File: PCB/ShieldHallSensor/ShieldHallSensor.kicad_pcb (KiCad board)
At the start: 2 copper layers, 34.2 x 34.2 mm, 8 parts, among them J1 Shield_Connector_Top_Left, J2 Shield_Connector_Bottom_Left, J3 Shield_Connector_Top_Right, J4 Shield_Connector_Bottom_Right, U1 HallLinearSensor

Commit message: Add smart cube panel
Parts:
- added REF**: Tab, PCM_kikit:Tab, F.Cu at (156.2, 97.0)
- added REF**: Tab, PCM_kikit:Tab, F.Cu at (138.9, 79.7)
- added REF**: Tab, PCM_kikit:Tab, F.Cu at (138.9, 114.3)
- added REF**: Tab, PCM_kikit:Tab, F.Cu at (121.6, 97.0)

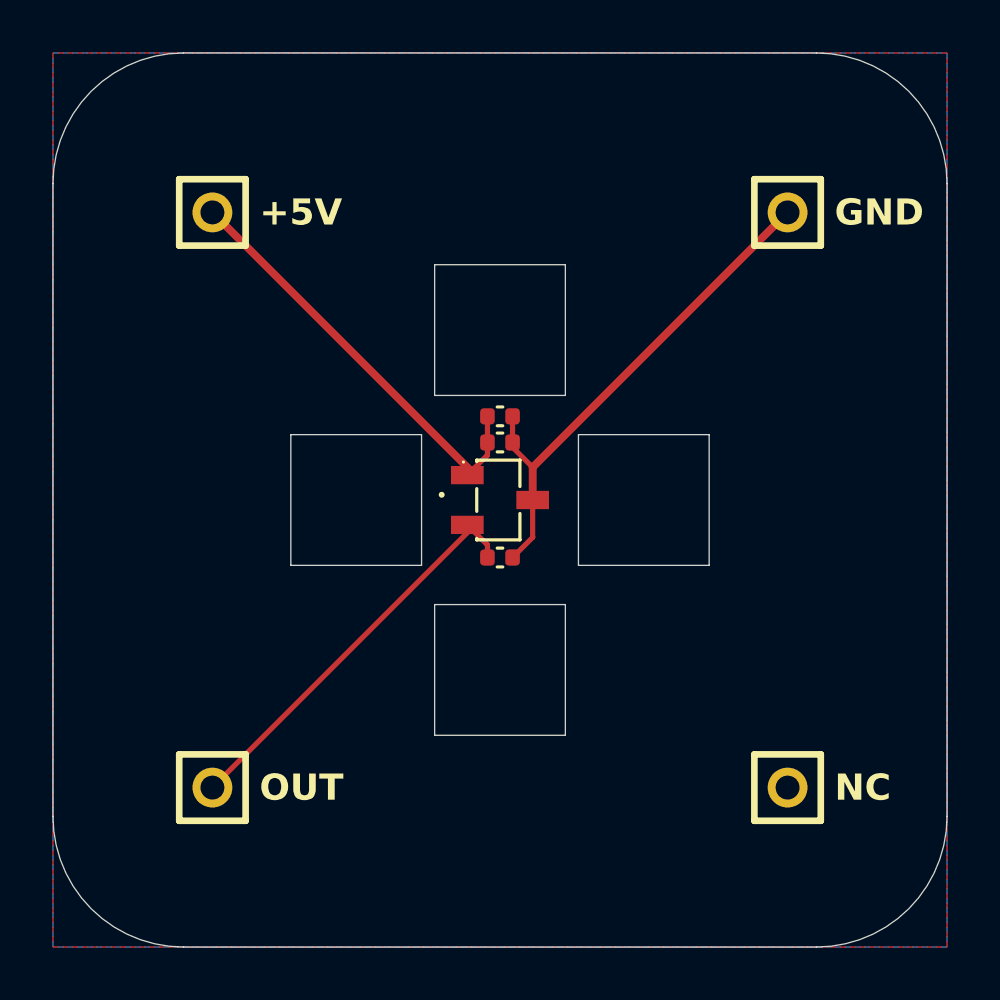
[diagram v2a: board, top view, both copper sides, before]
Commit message: Add power supply (wip) and update panel
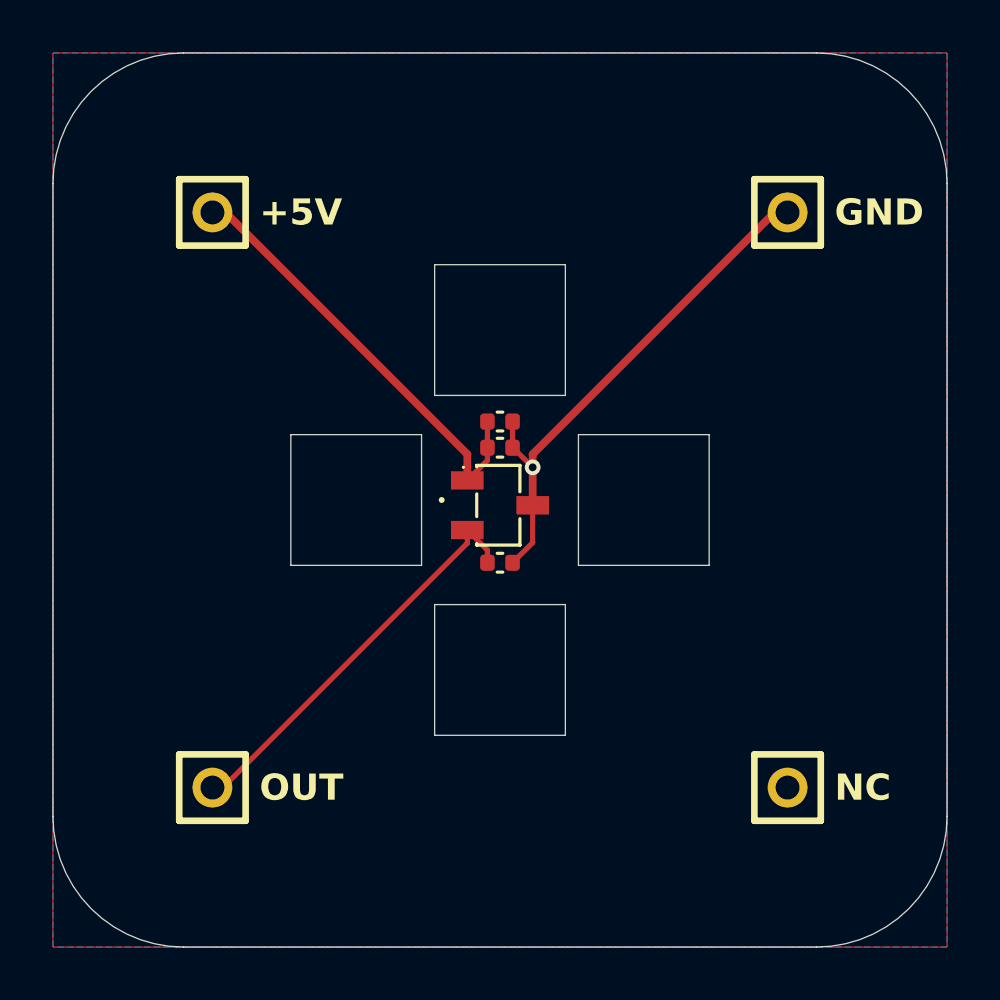
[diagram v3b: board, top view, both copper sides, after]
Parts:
- moved C1 0.20 mm to (138.9, 99.4)
- moved C2 0.20 mm to (138.9, 94.0)
- moved C3 0.20 mm to (138.9, 95.0)
- moved U1 0.20 mm to (138.9, 97.2)
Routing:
- net GND: track 19.8 -> 20.1 mm, vias 0 -> 1
- added copper zone on F.Cu, net +5V
- added copper zone on B.Cu, net GND
- removed copper zone on B.Cu, net (none)
- removed copper zone on F.Cu, net (none)
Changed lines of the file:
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@@
 	(footprint "Capacitor_SMD:C_0402_1005Metric"
 		(layer "F.Cu")
-		(at 138.940006 94.8)
+		(at 138.940006 95)
 		(descr "Capacitor SMD 0402 (1005 Metric), square (rectangular) end terminal, IPC_7351 nominal, (Body size source: IPC-SM-782 page 76, https://www.pcb-3d.com/wordpress/wp-content/uploads/ipc-sm-782a_amendment_1_and_2.pdf), generated with kicad-footprint-generator")
 		(tags "capacitor")
@@
 				(font
 					(size 1.27 1.27)
+					(thickness 0.15)
+				)
+			)
+		)
+		(property "LCSC" "C2883469"
+			(at 0 0 0)
+			(unlocked yes)
+			(layer "F.Fab")
+			(hide yes)
+			(effects
+				(font
+					(size 1 1)
 					(thickness 0.15)
 				)
@@
 	(footprint "Capacitor_SMD:C_0402_1005Metric"
 		(layer "F.Cu")
-		(at 138.940006 93.8)
+		(at 138.940006 94)
 		(descr "Capacitor SMD 0402 (1005 Metric), square (rectangular) end terminal, IPC_7351 nominal, (Body size source: IPC-SM-782 page 76, https://www.pcb-3d.com/wordpress/wp-content/uploads/ipc-sm-782a_amendment_1_and_2.pdf), generated with kicad-footprint-generator")
 		(tags "capacitor")
@@
 	(footprint "Capacitor_SMD:C_0402_1005Metric"
 		(layer "F.Cu")
-		(at 138.940006 99.2 180)
+		(at 138.940006 99.4 180)
 		(descr "Capacitor SMD 0402 (1005 Metric), square (rectangular) end terminal, IPC_7351 nominal, (Body size source: IPC-SM-782 page 76, https://www.pcb-3d.com/wordpress/wp-content/uploads/ipc-sm-782a_amendment_1_and_2.pdf), generated with kicad-footprint-generator")
 		(tags "capacitor")
@@
 				(font
 					(size 1.27 1.27)
+					(thickness 0.15)
+				)
+			)
+		)
+		(property "LCSC" "C2883469"
+			(at 0 0 0)
+			(unlocked yes)
+			(layer "F.Fab")
+			(hide yes)
+			(effects
+				(font
+					(size 1 1)
 					(thickness 0.15)
 				)
@@
 			)
 		)
+		(property "LCSC" "C2883469"
+			(at 0 0 0)
+			(unlocked yes)
+			(layer "F.Fab")
+			(hide yes)
+			(effects
+				(font
+					(size 1 1)
+					(thickness 0.15)
+				)
+			)
+		)
 		(property ki_fp_filters "Connector*:*_1x??_*")
 		(sheetname "Root")
@@
 			)
 		)
+		(property "LCSC" "C2883469"
+			(at 0 0 0)
+			(unlocked yes)
+			(layer "F.Fab")
+			(hide yes)
+			(effects
+				(font
+					(size 1 1)
+					(thickness 0.15)
+				)
+			)
+		)
 		(property ki_fp_filters "Connector*:*_1x??_*")
 		(sheetname "Root")
@@
 	(footprint "CustomFootprints:HallLinearSensor"
 		(layer "F.Cu")
-		(at 138.940006 97 180)
+		(at 138.940006 97.2 180)
 		(descr "SOT-23-3_L2.9-W1.6-P1.90-LS2.8-BR-CW footprint")
 		(tags "SOT-23-3_L2.9-W1.6-P1.90-LS2.8-BR-CW footprint C7420984")
@@
 	)
 	(segment
-		(start 138.460006 98.719644)
-		(end 137.690324 97.949962)
+		(start 138.460006 98.919644)
+		(end 137.690324 98.149962)
 		(width 0.2)
 		(layer "F.Cu")
@@
 	)
 	(segment
-		(start 127.940006 108)
-		(end 137.690324 98.249682)
+		(start 137.690324 98.649682)
+		(end 128.340006 108)
 		(width 0.2)
 		(layer "F.Cu")
@@
 	)
 	(segment
-		(start 137.690324 98.249682)
-		(end 137.690324 97.949962)
+		(start 128.340006 108)
+		(end 127.940006 108)
+		(width 0.2)
+		(layer "F.Cu")
+		(net 1)
+	)
+	(segment
+		(start 137.690324 98.149962)
+		(end 137.690324 98.649682)
 		(width 0.2)
 		(layer "F.Cu")
@@
 	(segment
 		(start 138.460006 99.2)
-		(end 138.460006 98.719644)
+		(end 138.460006 98.919644)
 		(width 0.2)
 		(layer "F.Cu")
@@
 	)
 	(segment
-		(start 140.189688 95.750318)
-		(end 140.189688 97)
-		(width 0.3)
-		(layer "F.Cu")
-		(net 3)
-	)
-	(segment
-		(start 149.940006 86)
-		(end 140.189688 95.750318)
+		(start 149.440006 86)
+		(end 149.940006 86)
 		(width 0.3)
 		(layer "F.Cu")
@@
 	)
 	(segment
-		(start 140.189688 98.430318)
-		(end 140.189688 97)
+		(start 140.189688 97.2)
+		(end 140.189688 98.630318)
 		(width 0.2)
 		(layer "F.Cu")
@@
 	)
 	(segment
-		(start 139.420006 93.8)
-		(end 139.420006 94.8)
-		(width 0.2)
-		(layer "F.Cu")
-		(net 3)
-	)
-	(segment
-		(start 139.420006 94.8)
+		(start 139.420006 94)
 		(end 139.420006 94.980636)
 		(width 0.2)
@@
 	)
 	(segment
-		(start 139.420006 99.2)
-		(end 140.189688 98.430318)
+		(start 140.189688 95.750318)
+		(end 140.189688 95.250318)
+		(width 0.3)
+		(layer "F.Cu")
+		(net 3)
+	)
+	(segment
+		(start 140.189688 95.250318)
+		(end 149.440006 86)
+		(width 0.3)
+		(layer "F.Cu")
+		(net 3)
+	)
+	(segment
+		(start 140.189688 98.630318)
+		(end 139.420006 99.4)
 		(width 0.2)
 		(layer "F.Cu")
@@
 	)
 	(segment
-		(start 138.460006 94.8)
-		(end 138.460006 93.8)
+		(start 140.189688 95.750318)
+		(end 140.189688 97.2)
+		(width 0.3)
+		(layer "F.Cu")
+		(net 3)
+	)
+	(via
+		(at 140.189688 95.750318)
+		(size 0.6)
+		(drill 0.3)
+		(layers "F.Cu" "B.Cu")
+		(net 3)
+	)
+	(segment
+		(start 137.690324 96.250038)
+		(end 138.460006 95.480356)
 		(width 0.2)
 		(layer "F.Cu")
@@
 	)
 	(segment
-		(start 127.940006 86)
-		(end 137.690324 95.750318)
+		(start 128.440006 86)
+		(end 127.940006 86)
 		(width 0.3)
 		(layer "F.Cu")
@@
 	)
 	(segment
-		(start 137.690324 95.750318)
-		(end 137.690324 96.050038)
+		(start 137.690324 95.250318)
+		(end 128.440006 86)
 		(width 0.3)
 		(layer "F.Cu")
@@
 	)
 	(segment
-		(start 138.460006 94.8)
-		(end 138.460006 95.280356)
+		(start 138.460006 95.480356)
+		(end 138.460006 94)
 		(width 0.2)
 		(layer "F.Cu")
@@
 	)
 	(segment
-		(start 138.460006 95.280356)
-		(end 137.690324 96.050038)
-		(width 0.2)
+		(start 137.690324 96.250038)
+		(end 137.690324 95.250318)
+		(width 0.3)
 		(layer "F.Cu")
 		(net 4)
 	)
 	(zone
-		(net 0)
-		(net_name "")
+		(net 4)
+		(net_name "+5V")
 		(layer "F.Cu")
 		(hatch edge 0.5)
@@
 	)
 	(zone
-		(net 0)
-		(net_name "")
+		(net 3)
+		(net_name "GND")
 		(layer "B.Cu")
 		(hatch edge 0.5)
